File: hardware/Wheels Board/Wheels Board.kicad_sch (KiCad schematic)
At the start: 0 parts

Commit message: current rev a
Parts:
- added C1: 10uf, symbol Device:C
- added C2, C3, C4: 100nf, symbol Device:C
- added J1: 53307-2471, UTSVT_Connectors:PeripheralSOM, symbol utsvt_connectors:PeripheralSOMConnector
- added J2: Conn_01x04, symbol Connector_Generic:Conn_01x04
- added J3: Conn_01x08_Pin, symbol Connector:Conn_01x08_Pin
- added J4: Conn_01x03, symbol Connector_Generic:Conn_01x03
- added R1, R2, R3, R4: 10k, symbol Device:R
- added U1: XIAO-ESP32-S3-SMD, XIAO-ESP32S3-SMD:XIAO-ESP32S3-SMD, symbol xiao-esp32s3-smd:XIAO-ESP32-S3-SMD
- added U2: ASM330LHHTR, LGA-14L_2P5X3X0P83_STM, symbol AIMU-SM330LHHTR:ASM330LHHTR
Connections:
- new net: J4.2 (Pin_2), R4.1
- new net: R3.2, U2.12 (CS)
- new net: C4.1, J4.1 (Pin_1)
- new net +24V: J1.24 (+24V_In)
- new net +3.3V: C1.1, C2.1, C3.1, J1.2 (+3.3v), J3.1 (Pin_1), R1.1, R2.1, R3.1, U1.12 (3V3), U2.5 (VDD_IO), U2.8 (VDD)
- new net +5V: U1.14 (5V)
- new net CAN_H: J1.22 (CAN_H), J2.3 (Pin_3)
- new net CAN_L: J1.20 (CAN_L), J2.2 (Pin_2)
- new net GND: C1.2, C2.2, C3.2, C4.2, J1.1 (GND), J1.3 (GND), J1.5 (GND), J3.2 (Pin_2), U1.13 (GND), U1.16 (GND), U2.6 (GND), U2.7 (GND)
- new net GNDA: J1.10 (GNDA)
- new net HALL_OUT: R4.2, U1.1 (GPIO1_A0_D0)
- new net IMU_SCL: J1.6 (I2C1_SCL), R2.2, U1.6 (GPIO6_A5_D5_SCL), U2.13 (SCL)
- new net IMU_SDA: J1.4 (I2C1_SDA), R1.2, U1.5 (GPIO5_A4_D4_SDA), U2.14 (SDA)
- new net INT: U2.4 (INT1)
- new net SCL: J3.3 (Pin_3)
- new net SDA: J3.4 (Pin_4)
- new net VDD: J4.3 (Pin_3)
- new net VDDA: J1.8 (VDDA)
- no-connect marks 0 -> 1
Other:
- note added: "6-AXIS IMU"
- note added: "CONNECTORS"
- note added: "PSOM CONNECTIONS"
- note added: "XIAO ESP32S3 MC"

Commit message: schematic v1
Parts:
- removed C4: 100nf, symbol Device:C
- removed J3: Conn_01x08_Pin, symbol Connector:Conn_01x08_Pin
- removed J4: Conn_01x03, symbol Connector_Generic:Conn_01x03
- removed R2, R3: 10k, symbol Device:R
- added C5: 100nf, symbol Device:C
- added D1, D2, D3: LED, symbol Device:LED
- added D5: MBR0520, Diode_SMD:D_SOD-123, symbol Diode:MBR0520
- added F1: Fuse, symbol Device:Fuse
- added J_BREAKOUTS: Conn_01x09, symbol Connector_Generic:Conn_01x09
- added J_HALL: Screw_Terminal_01x03, symbol Connector:Screw_Terminal_01x03
- added R5, R8: 10k, symbol Device:R
- added R6: 1.5k, symbol Device:R
- added R7: 82, symbol Device:R
- added TP, TP2, TP5: TestPoint, TestPoint:TestPoint_Pad_1.0x1.0mm, symbol Connector:TestPoint
- R4: value 10k -> 220
- renumbered J2 to J_CAN
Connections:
- net GNDA is gone; now on net GND: J1.10 (GNDA)
- net INT is gone; now on net IMU_INT1: U2.4 (INT1)
- net VDDA is gone; now on net +3.3V: J1.8 (VDDA)
- net +24V: now also J_CAN.4 (Pin_4), D1.2 (A)
- net +3.3V: now also D2.2 (A), TP2.1; no longer R1.1, U1.12 (3V3)
- net +5V: now also D3.2 (A), D5.2 (A), F1.1, TP5.1; no longer U1.14 (5V)
- net GND: now also J_CAN.1 (Pin_1), R1.2, R4.2, U1.20 (GND), U1.25 (PAD), U2.2 (RES), U2.3 (RES), C5.2, R6.2, R7.2, R8.2, TP.1
- net HALL_OUT: now also J1.11 (ADC1_IN9), J_BREAKOUTS.1 (Pin_1), R5.2; no longer R4.2, U1.1 (GPIO1_A0_D0)
- net ESP_SPI_MISO: now reaches U1.10 (GPIO8_A9_D9_MISO)
- net ESP_SPI_MISO: now also J1.14 (SPI2_MISO), J_BREAKOUTS.9 (Pin_9)
- net ESP_SPI_MOSI: now reaches U1.11 (GPIO9_A10_D10_MOSI)
- net ESP_SPI_MOSI: now also J1.16 (SPI2_MOSI), J_BREAKOUTS.8 (Pin_8)
- net ESP_SPI_SS: now reaches U1.4 (GPIO4_A3_D3)
- net ESP_SPI_SS: now also J1.12 (SPI2_NSS), J_BREAKOUTS.6 (Pin_6)
- net ESP_SPI_CLK: now reaches U1.9 (GPIO7_A8_D8_SCK)
- net ESP_SPI_CLK: now also J1.18 (SPI2_SCK), J_BREAKOUTS.7 (Pin_7)
- net IMU_INT1: now reaches J1.13 (ADC1_IN10)
- net IMU_INT1: now also R1.1
- net IMU_INT2: now reaches J1.15 (ADC1_IN11)
- net IMU_INT2: now also U2.9 (INT2), R8.1
- net IMU_SPI_MOSI: now reaches J1.17 (SPI1_MOSI)
- net IMU_SPI_MOSI: now also U2.14 (SDA), J_BREAKOUTS.4 (Pin_4)
- net IMU_SPI_SS: now reaches J1.19 (SPI1_NSS)
- net IMU_SPI_SS: now also U2.12 (CS), J_BREAKOUTS.2 (Pin_2)
- net IMU_SPI_MISO: now reaches J1.21 (SPI1_MISO)
- net IMU_SPI_MISO: now also U2.1 (SDO/SA0), J_BREAKOUTS.5 (Pin_5)
- net IMU_SPI_CLK: now reaches J1.23 (SPI1_SCK)
- net IMU_SPI_CLK: now also U2.13 (SCL), J_BREAKOUTS.3 (Pin_3)
- net at R4.1: now also D3.1 (K)
- removed net IMU_SCL: J1.6 (I2C1_SCL), U1.6 (GPIO6_A5_D5_SCL), U2.13 (SCL)
- removed net IMU_SDA: J1.4 (I2C1_SDA), R1.2, U1.5 (GPIO5_A4_D4_SDA), U2.14 (SDA)
- new net: D5.1 (K), U1.14 (5V)
- new net: D2.1 (K), R7.1
- new net: D1.1 (K), R6.1
- new net: F1.2, J_HALL.3 (Pin_3)
- new net: C5.1, J_HALL.1 (Pin_1)
- new net: J_HALL.2 (Pin_2), R5.1
- no-connect marks 1 -> 24
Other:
- added sheet 24v to 5v convertor (Voltage_Convertor.kicad_sch)
- note added: "BREAKOUTS"
- note added: "LEDS"
- note added: "TPS"
- note added: "probably dont need to breakout jtag"
- note added: "using adc as gpio"
- title: (none) -> Wheels Sensor Board
- moved on the sheet: C1, C2, C3, J1, J_CAN, U1, U2

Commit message: Rev a final draft
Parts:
- removed C5: 100nf, symbol Device:C
- removed F1: Fuse, symbol Device:Fuse
- removed J_BREAKOUTS: Conn_01x09, symbol Connector_Generic:Conn_01x09
- removed J_CAN: Conn_01x04, symbol Connector_Generic:Conn_01x04
- removed J_HALL: Screw_Terminal_01x03, symbol Connector:Screw_Terminal_01x03
- removed R5: 10k, symbol Device:R
- added C4: 100nf, symbol Device:C
- added F2: Fuse, symbol Device:Fuse
- added J2: MX150_02x04_Vertical, UTSVT_Connectors:CONN_SD-75757-002_2X04_F16p09_MOL, symbol utsvt_connectors:MX150_02x04_Vertical
- added R9: 10k, symbol Device:R
- U2: footprint LGA-14L_2P5X3X0P83_STM -> ASM330LHHTR-IMU:LGA-14L_2P5X3X0P83_STM
- renumbered TP2 to TP_3.3, TP5 to TP_5V1, TP to TP_GND1
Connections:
- net +24V: now also J2.1 (+24V)
- net +5V: now also F2.1
- net CAN_H: now also J2.2 (CANH_IN)
- net CAN_L: now also J2.3 (CANL_IN)
- net GND: now also C4.2, J2.5 (GND)
- net HALL_OUT: now also R9.2
- new net: F2.2, J2.6 (CANH_OUT)
- new net: J2.7 (CANL_OUT), R9.1
- new net: C4.1, J2.8 (GND_OUT*)
- no-connect marks 24 -> 25
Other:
- note added: "CONNECTOR"
- note removed: "BREAKOUTS"
- note removed: "CONNECTORS"
- note removed: "probably dont need to breakout jtag"
- moved on the sheet: D1, D2, D3, R4, R6, R7

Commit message: footprints
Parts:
- C1, C2, C3, C4: footprint (none) -> Capacitor_SMD:C_0805_2012Metric
- D1, D2, D3: footprint (none) -> LED_SMD:LED_WS2812B-2020_PLCC4_2.0x2.0mm
- F2: footprint (none) -> Fuse:Fuse_2920_7451Metric_Pad2.10x5.45mm_HandSolder
- R1, R4, R6, R7, R8, R9: footprint (none) -> Resistor_SMD:R_0603_1608Metric_Pad0.98x0.95mm_HandSolder
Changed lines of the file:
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@@
 			)
 		)
-		(property "Footprint" ""
+		(property "Footprint" "Capacitor_SMD:C_0805_2012Metric"
 			(at 107.6452 130.81 0)
 			(effects
@@
 			)
 		)
-		(property "Footprint" ""
+		(property "Footprint" "Resistor_SMD:R_0603_1608Metric_Pad0.98x0.95mm_HandSolder"
 			(at 146.812 181.61 90)
 			(effects
@@
 			)
 		)
-		(property "Footprint" ""
+		(property "Footprint" "LED_SMD:LED_WS2812B-2020_PLCC4_2.0x2.0mm"
 			(at 138.43 171.45 0)
 			(effects
@@
 			)
 		)
-		(property "Footprint" ""
+		(property "Footprint" "Resistor_SMD:R_0603_1608Metric_Pad0.98x0.95mm_HandSolder"
 			(at 264.922 83.82 90)
 			(effects
@@
 			)
 		)
-		(property "Footprint" ""
+		(property "Footprint" "Capacitor_SMD:C_0805_2012Metric"
 			(at 167.3352 115.57 0)
 			(effects
@@
 			)
 		)
-		(property "Footprint" ""
+		(property "Footprint" "LED_SMD:LED_WS2812B-2020_PLCC4_2.0x2.0mm"
 			(at 148.59 171.45 0)
 			(effects
@@
 			)
 		)
-		(property "Footprint" ""
+		(property "Footprint" "Resistor_SMD:R_0603_1608Metric_Pad0.98x0.95mm_HandSolder"
 			(at 136.652 181.61 90)
 			(effects
@@
 			)
 		)
-		(property "Footprint" ""
+		(property "Footprint" "Resistor_SMD:R_0603_1608Metric_Pad0.98x0.95mm_HandSolder"
 			(at 168.91 104.648 90)
 			(effects
@@
 			)
 		)
-		(property "Footprint" ""
+		(property "Footprint" "Resistor_SMD:R_0603_1608Metric_Pad0.98x0.95mm_HandSolder"
 			(at 254.762 85.09 90)
 			(effects
@@
 			)
 		)
-		(property "Footprint" ""
+		(property "Footprint" "LED_SMD:LED_WS2812B-2020_PLCC4_2.0x2.0mm"
 			(at 127 171.45 0)
 			(effects
@@
 			)
 		)
-		(property "Footprint" ""
+		(property "Footprint" "Fuse:Fuse_2920_7451Metric_Pad2.10x5.45mm_HandSolder"
 			(at 178.562 95.25 90)
 			(effects
@@
 			)
 		)
-		(property "Footprint" ""
+		(property "Footprint" "Capacitor_SMD:C_0805_2012Metric"
 			(at 96.2152 130.81 0)
 			(effects
@@
 			)
 		)
-		(property "Footprint" ""
+		(property "Footprint" "Capacitor_SMD:C_0805_2012Metric"
 			(at 35.2552 125.73 0)
 			(effects
@@
 			)
 		)
-		(property "Footprint" ""
+		(property "Footprint" "Resistor_SMD:R_0603_1608Metric_Pad0.98x0.95mm_HandSolder"
 			(at 125.222 181.61 90)
 			(effects

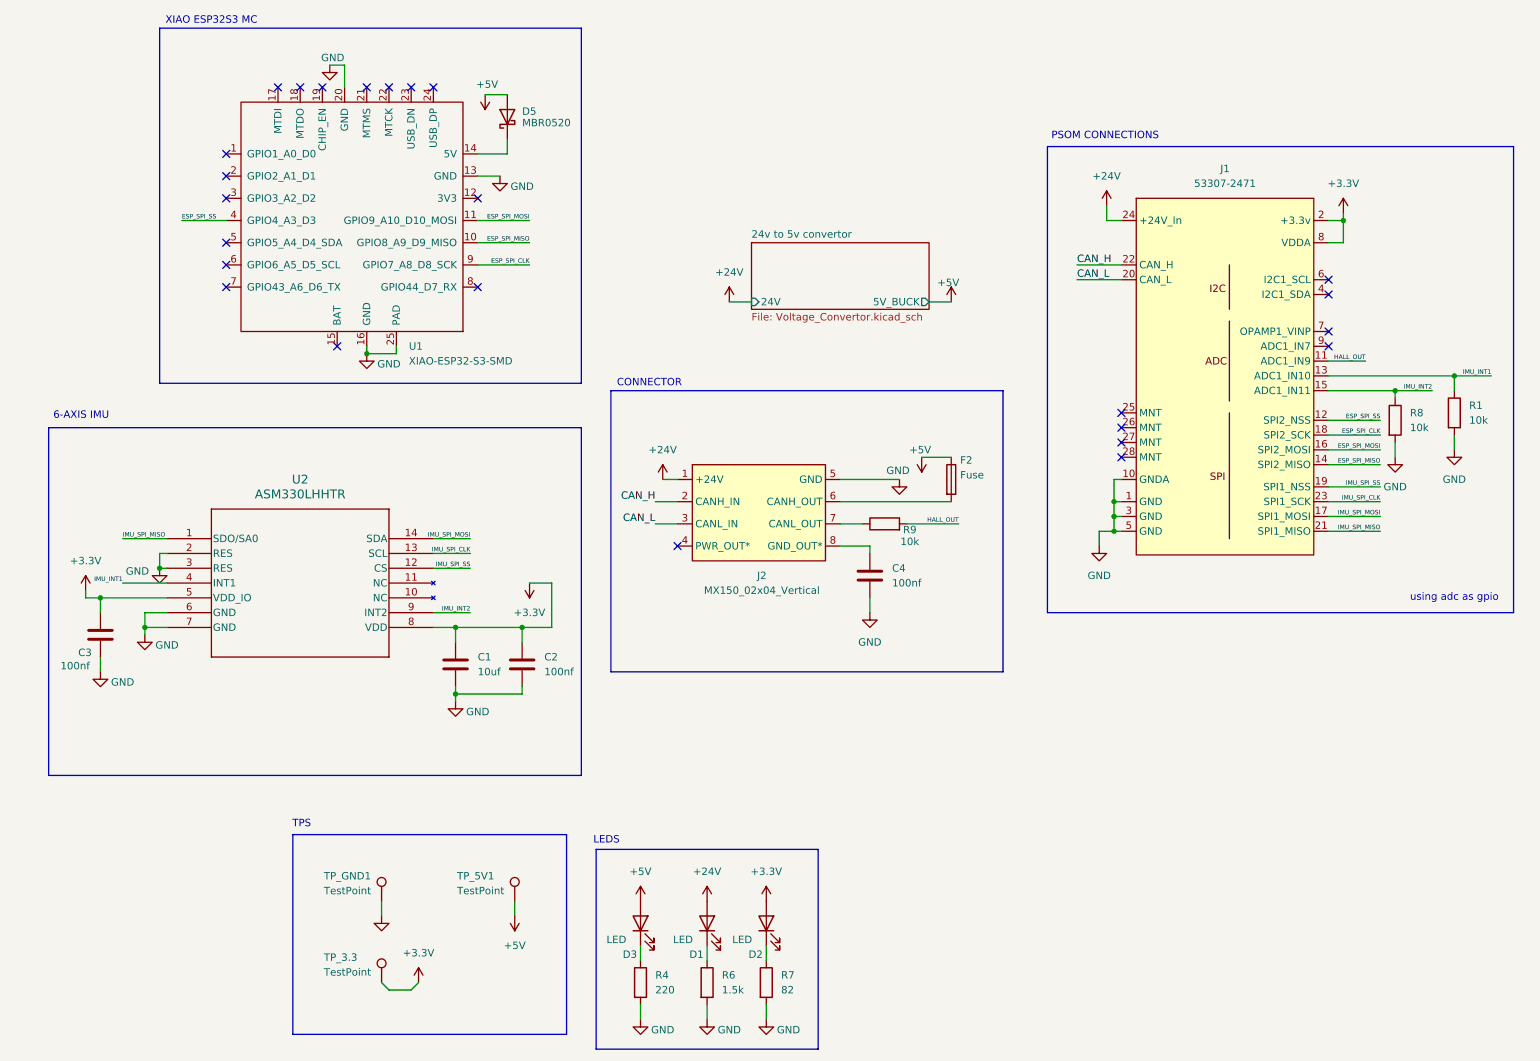
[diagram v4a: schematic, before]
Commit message: +op amp, breakout, footprints
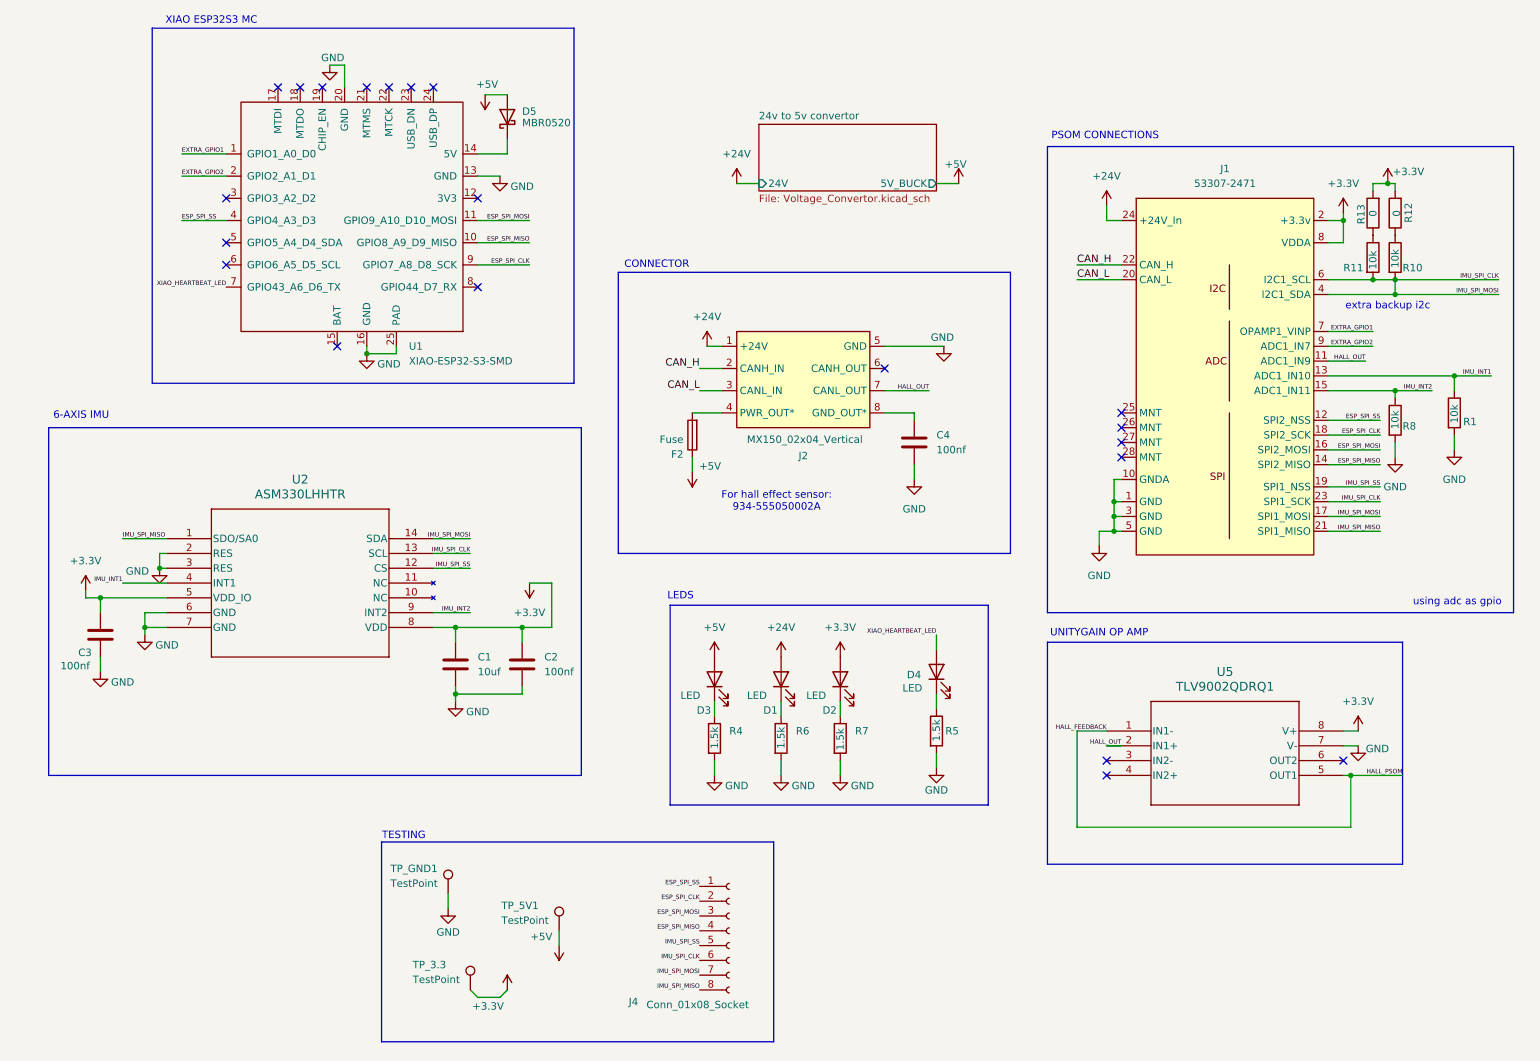
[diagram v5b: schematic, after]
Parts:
- removed R9: 10k, Resistor_SMD:R_0603_1608Metric_Pad0.98x0.95mm_HandSolder, symbol Device:R
- added D4: LED, LED_SMD:LED_0603_1608Metric_Pad1.05x0.95mm_HandSolder, symbol Device:LED
- added J4: Conn_01x08_Socket, Connector_PinHeader_2.54mm:PinHeader_1x08_P2.54mm_Vertical, symbol Connector:Conn_01x08_Socket
- added R10, R11: 10k, Resistor_SMD:R_0603_1608Metric_Pad0.98x0.95mm_HandSolder, symbol Device:R
- added R12, R13: 0, Resistor_SMD:R_0603_1608Metric_Pad0.98x0.95mm_HandSolder, symbol Device:R
- added R5: 1.5k, Resistor_SMD:R_0603_1608Metric_Pad0.98x0.95mm_HandSolder, symbol Device:R
- added U5: TLV9002QDRQ1, TLV9002QDRQ1:SOIC8_D_TEX, symbol TLV9002QDRQ1(Op-Amp):TLV9002QDRQ1
- C1: footprint Capacitor_SMD:C_0805_2012Metric -> Capacitor_SMD:C_0805_2012Metric_Pad1.18x1.45mm_HandSolder; P/N (none) -> GRM21BR61H106KE43K
- D1, D2, D3: footprint LED_SMD:LED_WS2812B-2020_PLCC4_2.0x2.0mm -> LED_SMD:LED_0603_1608Metric_Pad1.05x0.95mm_HandSolder; P/N (none) -> LTST-C193TBKT-5A
- R1, R8: P/N (none) -> CRCW060310K0FKEI
- R4: value 220 -> 1.5k; P/N (none) -> CRCW06032K00FKEA
- R6: P/N (none) -> CRCW06032K00FKEA
- R7: value 82 -> 1.5k; P/N (none) -> CRCW06032K00FKEA
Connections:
- net IMU_SPI_MOSI is gone; now on net IMU_SPI_CLK: J1.17 (SPI1_MOSI), U2.14 (SDA)
- net +3.3V: now also R12.2, R13.2, U5.8 (V+)
- net ESP_SPI_CLK: now also J4.2 (Pin_2)
- net ESP_SPI_MISO: now also J4.4 (Pin_4)
- net ESP_SPI_MOSI: now also J4.3 (Pin_3)
- net ESP_SPI_SS: now also J4.1 (Pin_1)
- net GND: now also R5.2, U5.7 (V-)
- net HALL_OUT: now also J2.7 (CANL_OUT), U5.2 (IN1+)
- net IMU_SPI_CLK: now also J1.4 (I2C1_SDA), J1.6 (I2C1_SCL), J4.6 (Pin_6), J4.7 (Pin_7), R10.2, R11.2
- net IMU_SPI_MISO: now also J4.8 (Pin_8)
- net IMU_SPI_SS: now also J4.5 (Pin_5)
- net at J2.4 (PWR_OUT*): now also F2.2
- net at J2.6 (CANH_OUT): no longer F2.2
- net EXTRA_GPIO1: now reaches U1.1 (GPIO1_A0_D0)
- net EXTRA_GPIO1: now also J1.7 (OPAMP1_VINP)
- net EXTRA_GPIO2: now reaches U1.2 (GPIO2_A1_D1)
- net EXTRA_GPIO2: now also J1.9 (ADC1_IN7)
- net XIAO_HEARTBEAT_LED: now reaches U1.7 (GPIO43_A6_D6_TX)
- net XIAO_HEARTBEAT_LED: now also D4.2 (A)
- new net: R11.1, R13.1
- new net: D4.1 (K), R5.1
- new net: R10.1, R12.1
- new net HALL_FEEDBACK: U5.1 (IN1-), U5.5 (OUT1)
- no-connect marks 25 -> 21
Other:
- note added: "For hall effect sensor: 934-555050002A"
- note added: "TESTING"
- note added: "UNITYGAIN OP AMP"
- note added: "extra backup i2c"
- note removed: "TPS"
- moved on the sheet: C4, D1, D2, D3, F2, J2, R4, R6, R7, TP_3.3, TP_5V1, TP_GND1

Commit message: switched to pads for hall sensor wires
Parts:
- added TP_5V, TP_GND, TP_OUT: HallPad, TestPoint:TestPoint_Pad_1.0x1.0mm, symbol Connector:TestPoint
- C1: footprint Capacitor_SMD:C_0805_2012Metric_Pad1.18x1.45mm_HandSolder -> Capacitor_SMD:C_0603_1608Metric_Pad1.08x0.95mm_HandSolder
- C2, C3, C4: footprint Capacitor_SMD:C_0805_2012Metric -> Capacitor_SMD:C_0603_1608Metric_Pad1.08x0.95mm_HandSolder
- D5: footprint Diode_SMD:D_SOD-123 -> Diode_SMD:D_SOD-323_HandSoldering
- F2: footprint Fuse:Fuse_2920_7451Metric_Pad2.10x5.45mm_HandSolder -> Fuse:FUSE_3568
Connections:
- net HALL_OUT: now also TP_OUT.1; no longer J2.7 (CANL_OUT)
- net at J2.4 (PWR_OUT*): no longer F2.2
- net at C4.1: now also TP_GND.1; no longer J2.8 (GND_OUT*)
- new net: F2.2, TP_5V.1
- no-connect marks 21 -> 24
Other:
- note added: "Pads for hall effect sensor: 934-555050002A"
- note removed: "For hall effect sensor: 934-555050002A"
- moved on the sheet: C4, D1, D2, D3, D4, F2, J1, J2, J4, R1, R10, R11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

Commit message: layout planning
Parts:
- renumbered TP_5V to TP_5V2, TP_GND to TP_GND2, TP_OUT to TP_OUT1
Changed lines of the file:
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@@
 		(on_board yes)
 		(dnp no)
-		(property "Reference" "TP_GND"
+		(property "Reference" "TP_GND2"
 			(at 67.056 176.784 90)
 			(effects
@@
 			(project "Wheels Board"
 				(path "/ef02af58-69c4-4999-88e2-94274884d34c"
-					(reference "TP_GND")
+					(reference "TP_GND2")
 					(unit 1)
 				)
@@
 		(on_board yes)
 		(dnp no)
-		(property "Reference" "TP_5V"
+		(property "Reference" "TP_5V2"
 			(at 67.056 166.624 90)
 			(effects
@@
 			(project "Wheels Board"
 				(path "/ef02af58-69c4-4999-88e2-94274884d34c"
-					(reference "TP_5V")
+					(reference "TP_5V2")
 					(unit 1)
 				)
@@
 		(on_board yes)
 		(dnp no)
-		(property "Reference" "TP_OUT"
+		(property "Reference" "TP_OUT1"
 			(at 67.056 171.704 90)
 			(effects
@@
 			(project "Wheels Board"
 				(path "/ef02af58-69c4-4999-88e2-94274884d34c"
-					(reference "TP_OUT")
-					(unit 1)
-				)
+					(reference "TP_OUT1")
+					(unit 1)
+				)

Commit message: added uart to sch
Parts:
- removed R10, R11: 10k, Resistor_SMD:R_0603_1608Metric_Pad0.98x0.95mm_HandSolder, symbol Device:R
- removed R12, R13: 0, Resistor_SMD:R_0603_1608Metric_Pad0.98x0.95mm_HandSolder, symbol Device:R
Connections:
- net IMU_SPI_CLK: no longer J1.17 (SPI1_MOSI), J1.4 (I2C1_SDA), J1.6 (I2C1_SCL), J4.7 (Pin_7), U2.14 (SDA)
- net XIAO_HEARTBEAT_LED: now also U1.3 (GPIO3_A2_D2); no longer U1.7 (GPIO43_A6_D6_TX)
- net ESP_UART_RX: now reaches U1.8 (GPIO44_D7_RX)
- net ESP_UART_RX: now also J1.4 (I2C1_SDA)
- new net ESP_UART_TX: J1.6 (I2C1_SCL), U1.7 (GPIO43_A6_D6_TX)
- new net IMU_SPI_MOSI: J1.17 (SPI1_MOSI), J4.7 (Pin_7), U2.14 (SDA)
- no-connect marks 24 -> 22
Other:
- note removed: "extra backup i2c"
